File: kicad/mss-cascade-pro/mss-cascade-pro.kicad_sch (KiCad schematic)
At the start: 123 parts, among them J1 Molex 0532610471, J10 Screw_Terminal_01x02, J11 Molex 0532610471, J12 Molex 0532610471, J13 8P8C, J15 SM04B-SRSS, J16 SM04B-SRSS, J17 SM04B-SRSS, J18 AVR-ISP, J2 Molex 0532610471, J3 Screw_Terminal_01x02, J5 Screw_Terminal_01x02, J6 Screw_Terminal_01x02, J7 Screw_Terminal_01x02, J8 8P8C, J9 Screw_Terminal_01x02, SW1 JS202011SCQN, SW2 JS202011SCQN, U1 AP7381-50Y, U2 AP3012, U3 74HC4049, U4 74HC4049, U5 PCA9555PW, U6 ATtiny861A-S

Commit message: Continued work on cascade pro
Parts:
- gave numbers to parts that had none: 2
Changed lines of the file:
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@@
   (symbol (lib_id "Device:R_US") (at 258.445 138.43 90) (unit 1)
     (in_bom yes) (on_board yes)
-    (property "Reference" "R?" (id 0) (at 260.35 135.89 90))
+    (property "Reference" "R1" (id 0) (at 260.35 135.89 90))
     (property "Value" "10k" (id 1) (at 256.54 135.89 90))
     (property "Footprint" "Resistor_SMD:R_0805_2012Metric" (id 2) (at 258.699 137.414 90)
@@
   (symbol (lib_id "power:+5V") (at 31.115 59.055 0) (unit 1)
     (in_bom yes) (on_board yes) (fields_autoplaced)
-    (property "Reference" "#PWR?" (id 0) (at 31.115 62.865 0)
+    (property "Reference" "#PWR0106" (id 0) (at 31.115 62.865 0)
       (effects (font (size 1.27 1.27)) hide)
     )
@@
   (symbol (lib_id "power:+12V") (at 285.115 127.635 0) (mirror y) (unit 1)
     (in_bom yes) (on_board yes)
-    (property "Reference" "#PWR?" (id 0) (at 285.115 131.445 0)
+    (property "Reference" "#PWR0102" (id 0) (at 285.115 131.445 0)
       (effects (font (size 1.27 1.27)) hide)
     )
@@
   (symbol (lib_id "power:GND") (at 144.145 250.19 0) (unit 1)
     (in_bom yes) (on_board yes)
-    (property "Reference" "#PWR?" (id 0) (at 144.145 256.54 0)
+    (property "Reference" "#PWR0105" (id 0) (at 144.145 256.54 0)
       (effects (font (size 1.27 1.27)) hide)
     )
@@
   (symbol (lib_id "power:GND") (at 74.93 33.02 0) (unit 1)
     (in_bom yes) (on_board yes)
-    (property "Reference" "#PWR?" (id 0) (at 74.93 39.37 0)
+    (property "Reference" "#PWR0107" (id 0) (at 74.93 39.37 0)
       (effects (font (size 1.27 1.27)) hide)
     )
@@
   (symbol (lib_id "power:GND") (at 324.485 150.495 0) (unit 1)
     (in_bom yes) (on_board yes)
-    (property "Reference" "#PWR?" (id 0) (at 324.485 156.845 0)
+    (property "Reference" "#PWR0101" (id 0) (at 324.485 156.845 0)
       (effects (font (size 1.27 1.27)) hide)
     )
@@
   (symbol (lib_id "Switch:SW_DIP_x08") (at 151.765 234.95 180) (unit 1)
     (in_bom yes) (on_board yes)
-    (property "Reference" "SW?" (id 0) (at 151.765 221.615 0))
+    (property "Reference" "SW3" (id 0) (at 151.765 221.615 0))
     (property "Value" "SW_DIP_x08" (id 1) (at 151.765 223.52 0))
     (property "Footprint" "Button_Switch_SMD:SW_DIP_SPSTx08_Slide_6.7x21.88mm_W8.61mm_P2.54mm_LowProfile" (id 2) (at 151.765 234.95 0)
@@
   (symbol (lib_id "power:GND") (at 116.84 247.015 0) (unit 1)
     (in_bom yes) (on_board yes)
-    (property "Reference" "#PWR?" (id 0) (at 116.84 253.365 0)
+    (property "Reference" "#PWR0104" (id 0) (at 116.84 253.365 0)
       (effects (font (size 1.27 1.27)) hide)
     )
@@
       (reference "#PWR052") (unit 1) (value "GND") (footprint "")
     )
+    (path "/b2082e18-dbb8-44e5-8f0d-a91bab4668da"
+      (reference "#PWR0101") (unit 1) (value "GND") (footprint "")
+    )
+    (path "/88d00145-d61e-4f9b-9262-3c2cfdd5b878"
+      (reference "#PWR0102") (unit 1) (value "+12V") (footprint "")
+    )
     (path "/d3f56b2e-499a-4942-8ff9-230574ce708e"
       (reference "#PWR0103") (unit 1) (value "GND") (footprint "")
     )
+    (path "/bd9c16ed-ef8d-4f91-93ed-dd683129e000"
+      (reference "#PWR0104") (unit 1) (value "GND") (footprint "")
+    )
+    (path "/9b79d4c0-d920-4c8f-8d9c-aed433ce5d68"
+      (reference "#PWR0105") (unit 1) (value "GND") (footprint "")
+    )
     (path "/5ccd9c99-28ad-41c9-8e0f-8705affab77d"
-      (reference "#PWR?") (unit 1) (value "+5V") (footprint "")
-    )
-    (path "/88d00145-d61e-4f9b-9262-3c2cfdd5b878"
-      (reference "#PWR?") (unit 1) (value "+12V") (footprint "")
-    )
-    (path "/9b79d4c0-d920-4c8f-8d9c-aed433ce5d68"
-      (reference "#PWR?") (unit 1) (value "GND") (footprint "")
+      (reference "#PWR0106") (unit 1) (value "+5V") (footprint "")
     )
     (path "/b0088712-f6dc-4769-af51-21d22f19bfe2"
-      (reference "#PWR?") (unit 1) (value "GND") (footprint "")
-    )
-    (path "/b2082e18-dbb8-44e5-8f0d-a91bab4668da"
-      (reference "#PWR?") (unit 1) (value "GND") (footprint "")
-    )
-    (path "/bd9c16ed-ef8d-4f91-93ed-dd683129e000"
-      (reference "#PWR?") (unit 1) (value "GND") (footprint "")
+      (reference "#PWR0107") (unit 1) (value "GND") (footprint "")
     )
     (path "/f7afeb96-08a7-44d0-9778-892656948ff0"
@@
       (reference "L2") (unit 1) (value "4.7uH") (footprint "ISE_UltraLibrarian:MSS6132-xxxMLC")
     )
+    (path "/44d42cfd-1473-4354-a700-d5c11b16e27c"
+      (reference "R1") (unit 1) (value "10k") (footprint "Resistor_SMD:R_0805_2012Metric")
+    )
     (path "/eb833c4d-054d-4f37-92c2-564f5eea5e87"
       (reference "R3") (unit 1) (value "330") (footprint "Resistor_SMD:R_0805_2012Metric")
@@
       (reference "R40") (unit 1) (value "10k") (footprint "Resistor_SMD:R_0805_2012Metric")
     )
-    (path "/44d42cfd-1473-4354-a700-d5c11b16e27c"
-      (reference "R?") (unit 1) (value "10k") (footprint "Resistor_SMD:R_0805_2012Metric")
-    )
     (path "/a456ff59-9866-4634-a18c-c4c411e7d7e9"
       (reference "SW1") (unit 1) (value "JS202011SCQN") (footprint "ISE_UltraLibrarian:SW_JS202011SCQN")
@@
     )
     (path "/ba2acef0-547c-4ec8-b17d-2cea016e647d"
-      (reference "SW?") (unit 1) (value "SW_DIP_x08") (footprint "Button_Switch_SMD:SW_DIP_SPSTx08_Slide_6.7x21.88mm_W8.61mm_P2.54mm_LowProfile")
+      (reference "SW3") (unit 1) (value "SW_DIP_x08") (footprint "Button_Switch_SMD:SW_DIP_SPSTx08_Slide_6.7x21.88mm_W8.61mm_P2.54mm_LowProfile")
     )
     (path "/c88d7df6-3504-4ee5-8948-e01ccd277842"

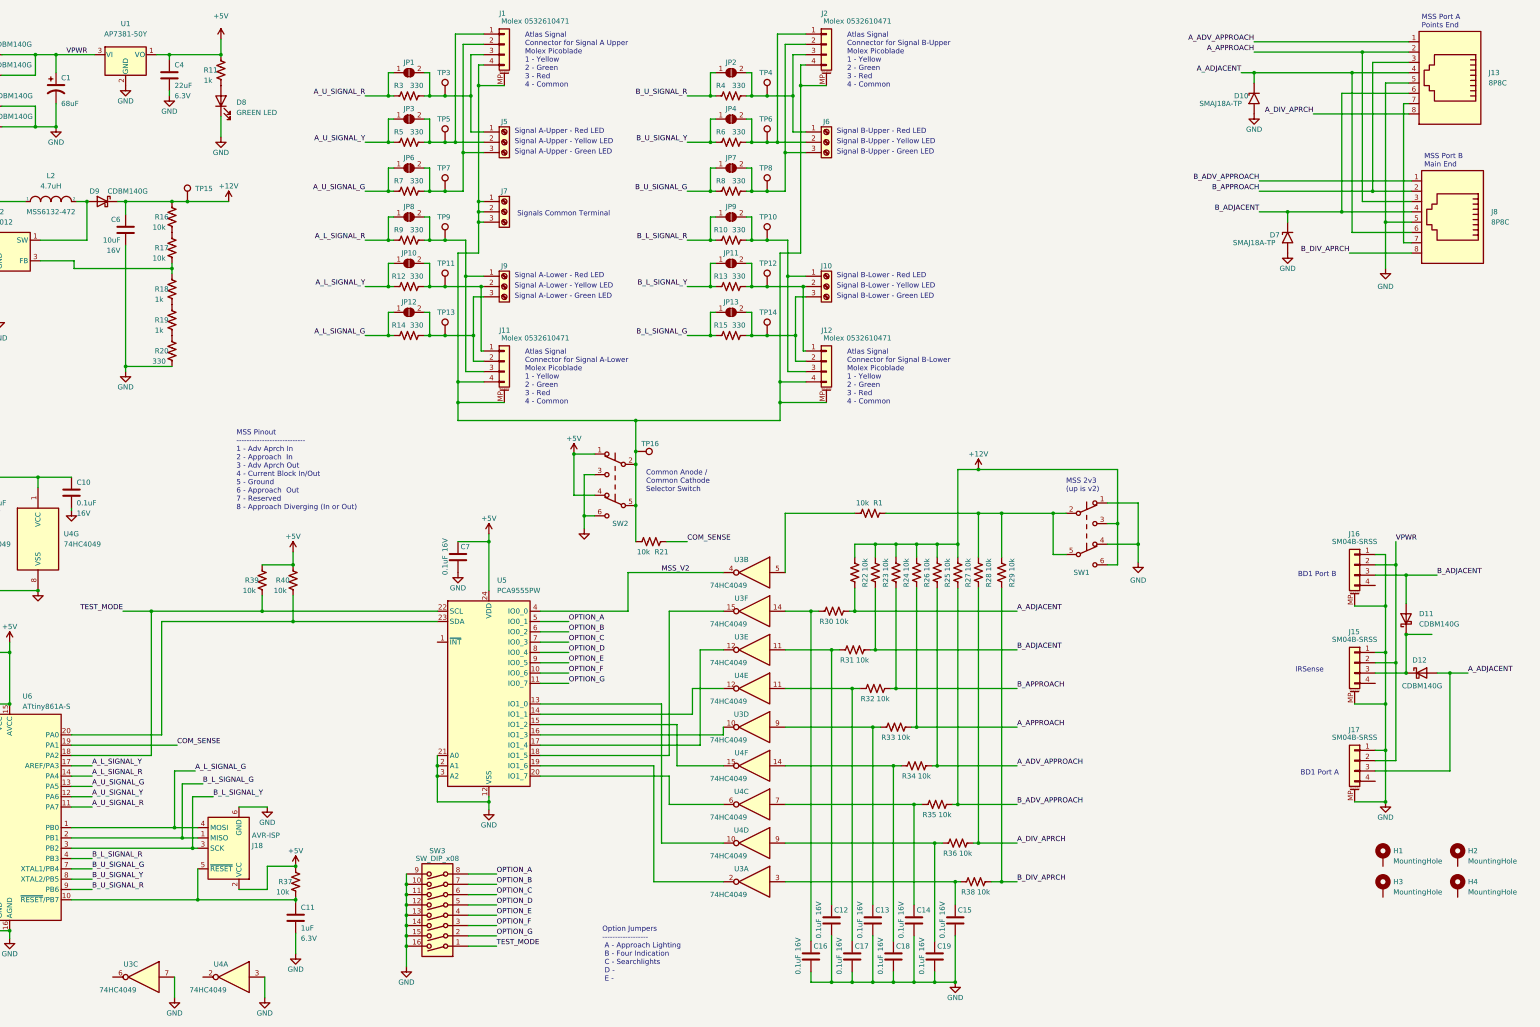
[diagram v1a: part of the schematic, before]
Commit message: Initial cut of the cascade pro idea
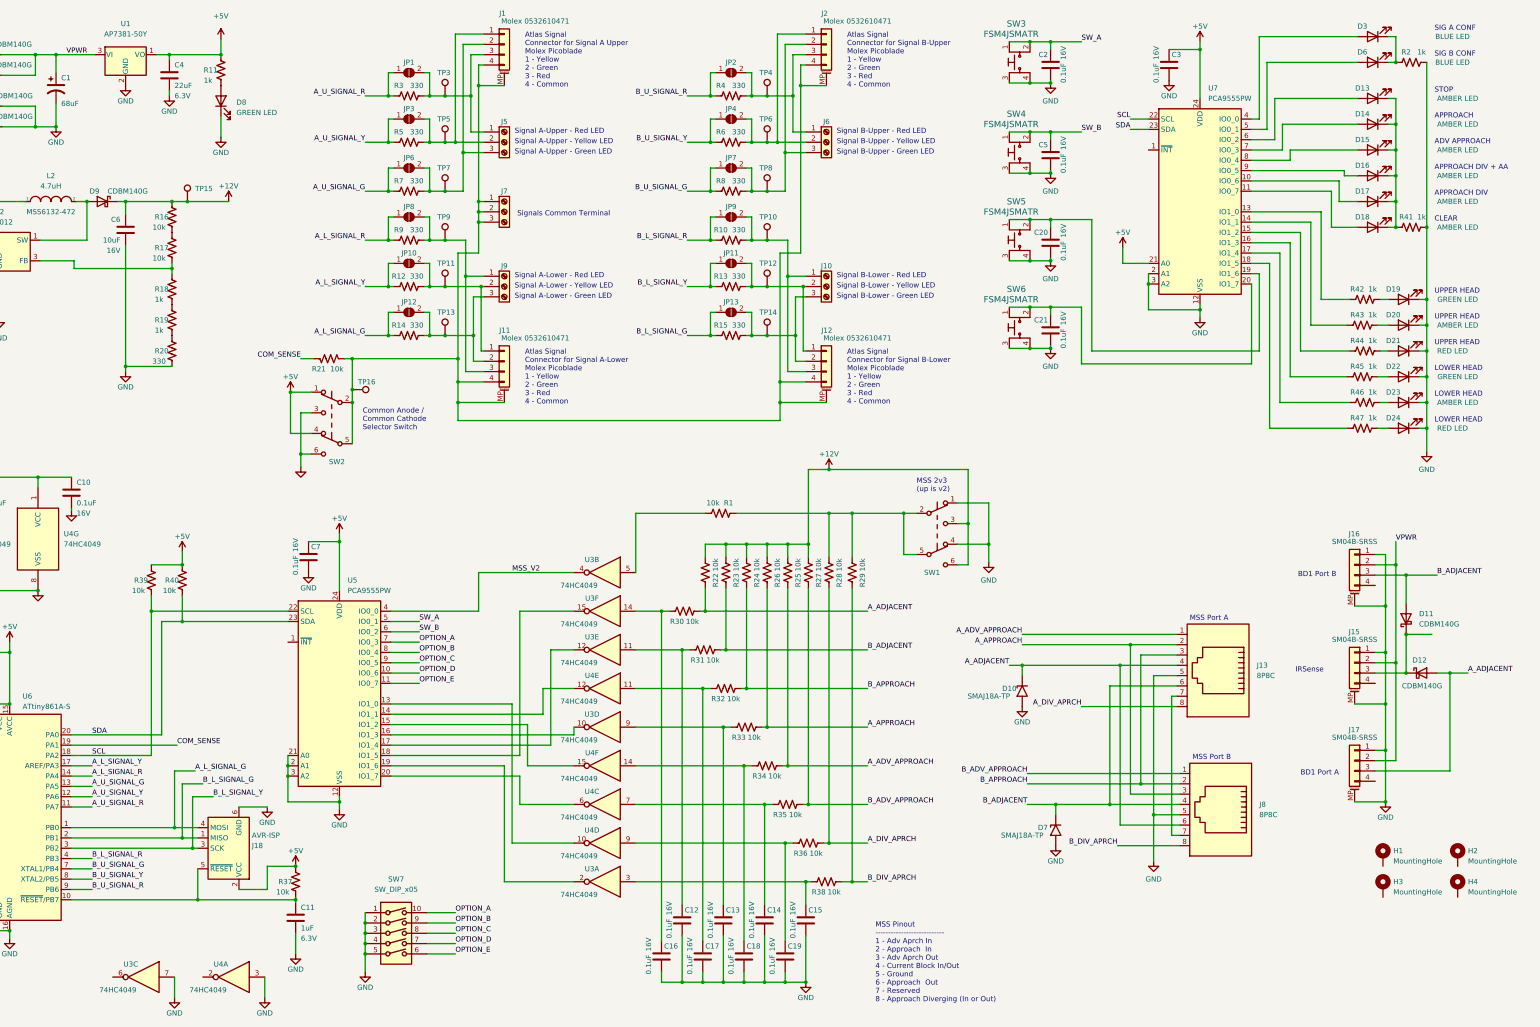
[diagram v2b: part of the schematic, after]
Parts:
- removed SW3: SW_DIP_x08, Button_Switch_SMD:SW_DIP_SPSTx08_Slide_6.7x21.88mm_W8.61mm_P2.54mm_LowProfile, symbol Switch:SW_DIP_x08
- added C2, C20, C21, C3, C5: 0.1uF, Capacitor_SMD:C_0805_2012Metric, symbol Device:C
- added D13, D14, D15, D16, D17, D18, D20, D23: AMBER LED, LED_SMD:LED_0805_2012Metric, symbol Device:LED
- added D19, D22: GREEN LED, LED_SMD:LED_0805_2012Metric, symbol Device:LED
- added D21, D24: RED LED, LED_SMD:LED_0805_2012Metric, symbol Device:LED
- added D3, D6: BLUE LED, LED_SMD:LED_0805_2012Metric, symbol Device:LED
- added R2, R41, R42, R43, R44, R45, R46, R47: 1k, Resistor_SMD:R_0805_2012Metric, symbol Device:R_US
- added SW3, SW4, SW5, SW6: FSM4JSMATR, ISE_Generic:TE_FSM4JSMA, symbol dk_Tactile-Switches:FSM4JSMATR
- added SW7: SW_DIP_x05, Button_Switch_SMD:SW_DIP_SPSTx05_Slide_6.7x14.26mm_W8.61mm_P2.54mm_LowProfile, symbol Switch:SW_DIP_x05
- added U7: PCA9555PW, Package_SO:TSSOP-24_4.4x7.8mm_P0.65mm, symbol Interface_Expansion:PCA9555PW
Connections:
- net OPTION_F is gone; now on net OPTION_D: U5.10 (IO0_6)
- net OPTION_G is gone; now on net OPTION_E: U5.11 (IO0_7)
- net +5V: now also C3.1, U7.21 (A0), U7.24 (VDD)
- net GND: now also C2.2, C20.2, C21.2, C3.2, C5.2, D19.1 (K), D20.1 (K), D21.1 (K), D22.1 (K), D23.1 (K), D24.1 (K), R2.2, R41.2, SW3.3, SW3.4, SW4.3, SW4.4, SW5.3, SW5.4, SW6.3, SW6.4, SW7.1, SW7.2, SW7.3, SW7.4, SW7.5, U7.12 (VSS), U7.2 (A1), U7.3 (A2)
- net OPTION_A: now also U5.7 (IO0_3), SW7.10; no longer U5.5 (IO0_1)
- net OPTION_B: now also U5.8 (IO0_4), SW7.9; no longer U5.6 (IO0_2)
- net OPTION_C: now also U5.9 (IO0_5), SW7.8; no longer U5.7 (IO0_3)
- net OPTION_D: now also SW7.7; no longer U5.8 (IO0_4)
- net OPTION_E: now also SW7.6; no longer U5.9 (IO0_5)
- net SDA: now reaches R40.1, U5.23 (SDA), U6.20 (PA0)
- net SDA: now also U7.23 (SDA)
- net TEST_MODE renamed SCL
- net SCL: now also U7.22 (SCL)
- new net: D3.1 (K), D6.1 (K), R2.1
- new net: D6.2 (A), U7.5 (IO0_1)
- new net: R43.1, U7.14 (IO1_1)
- new net: D20.2 (A), R43.2
- new net: D13.1 (K), D14.1 (K), D15.1 (K), D16.1 (K), D17.1 (K), D18.1 (K), R41.1
- new net: D17.2 (A), U7.10 (IO0_6)
- new net: R45.1, U7.16 (IO1_3)
- new net: D22.2 (A), R45.2
- new net: R42.1, U7.13 (IO1_0)
- new net: D19.2 (A), R42.2
- new net: D15.2 (A), U7.8 (IO0_4)
- new net: D24.2 (A), R47.2
- new net: R44.1, U7.15 (IO1_2)
- new net: D21.2 (A), R44.2
- new net: C20.1, SW5.1, SW5.2, U7.19 (IO1_6)
- new net: D13.2 (A), U7.6 (IO0_2)
- new net: R47.1, U7.18 (IO1_5)
- new net: D3.2 (A), U7.4 (IO0_0)
- new net: D18.2 (A), U7.11 (IO0_7)
- new net: R46.1, U7.17 (IO1_4)
- new net: C21.1, SW6.1, SW6.2, U7.20 (IO1_7)
- new net: D14.2 (A), U7.7 (IO0_3)
- new net: D16.2 (A), U7.9 (IO0_5)
- new net: D23.2 (A), R46.2
- new net SW_A: C2.1, SW3.1, SW3.2, U5.5 (IO0_1)
- new net SW_B: C5.1, SW4.1, SW4.2, U5.6 (IO0_2)
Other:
- note added: "ADV APPROACH"
- note added: "APPROACH"
- note added: "APPROACH DIV"
- note added: "APPROACH DIV + AA"
- note added: "CLEAR"
- note added: "LOWER HEAD"
- note added: "MSS Port A"
- note added: "MSS Port B"
- note added: "SIG A CONF"
- note added: "SIG B CONF"
- note added: "STOP"
- note added: "UPPER HEAD"
- note removed: "MSS Port A Points End"
- note removed: "MSS Port B Main End"
- note removed: "Option Jumpers ------------------ A - Approach Lighting B - Four Indication C - Searchlights D - E -"
- moved on the sheet: C12, C13, C14, C15, C16, C17, C18, C19, C7, D10, D7, J13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
